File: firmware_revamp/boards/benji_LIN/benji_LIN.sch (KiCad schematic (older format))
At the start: 35 parts, among them J1 CONN_02X03, J2 Conn_01x11, J3 Conn_01x11, U1 MCP2561-E_SN, U2 ATMEGA16M1, U3 TLIN1021DRQ1, Y1 Crystal_SMD

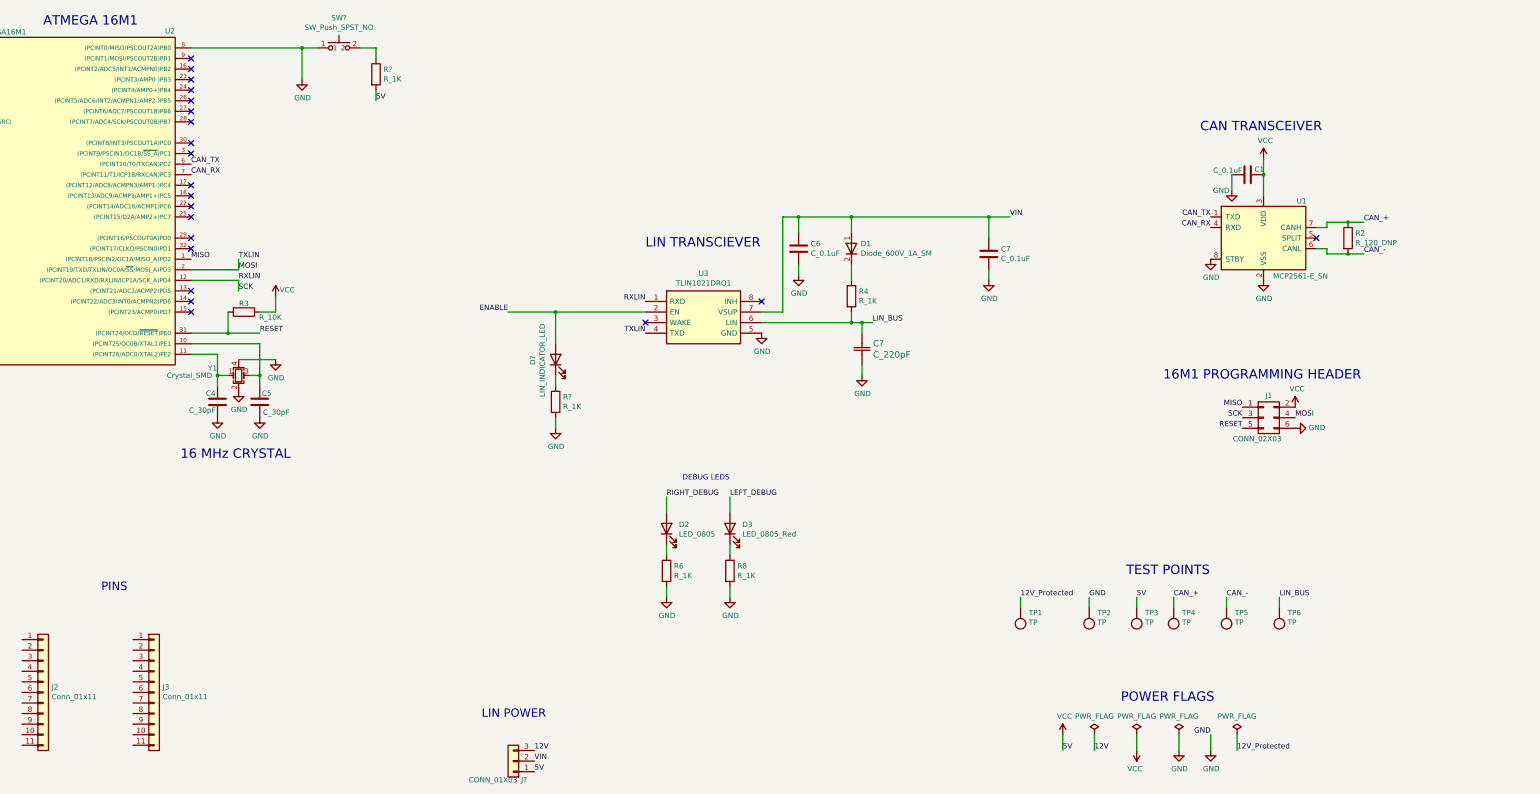
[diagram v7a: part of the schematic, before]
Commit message: Changed test points to smd
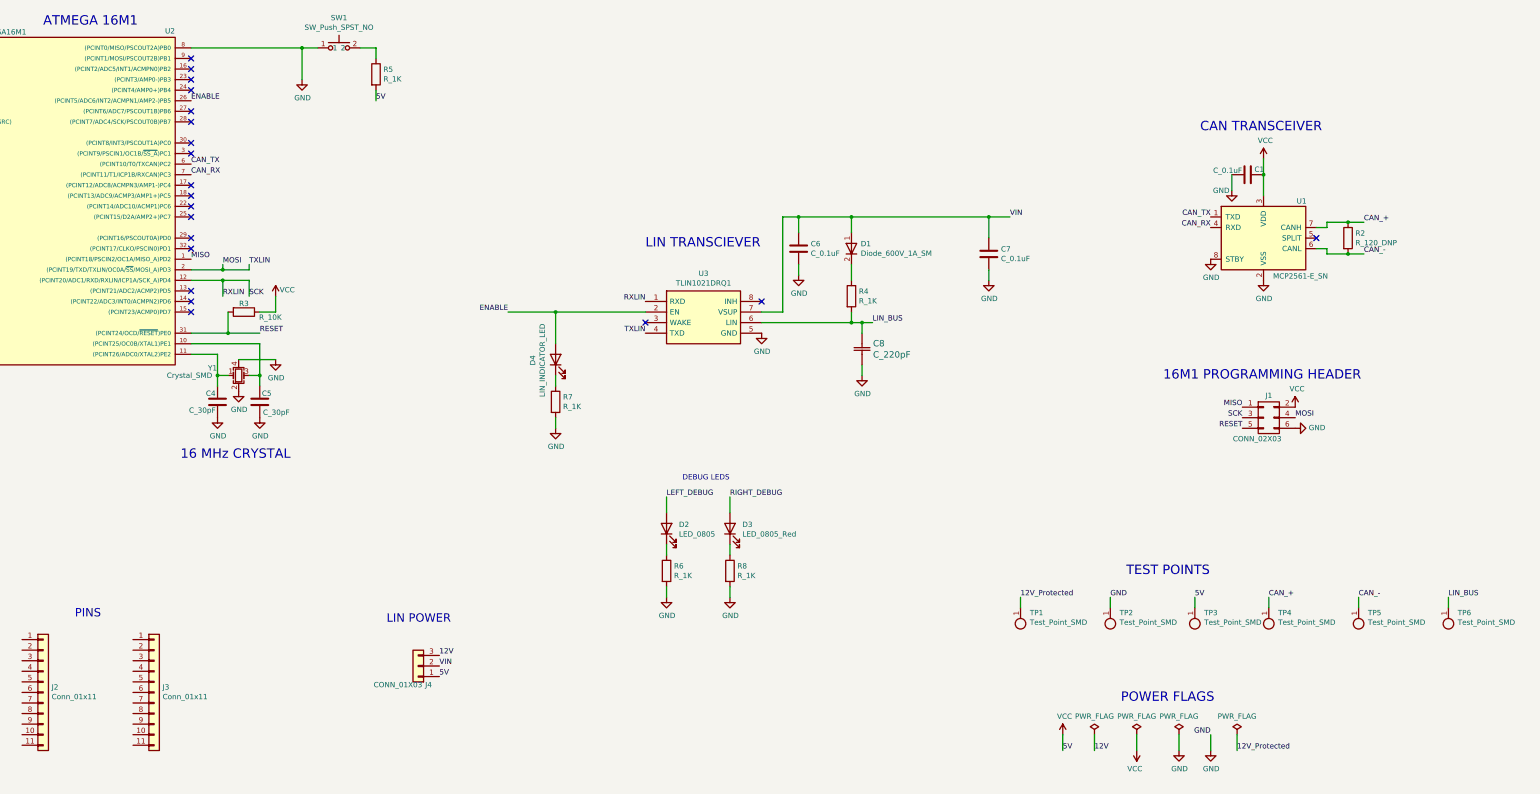
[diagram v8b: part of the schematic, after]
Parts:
- removed TP1, TP2, TP3, TP4, TP5, TP6: TP, footprints:tp_1.6mm, symbol formula:TP
- added TP1, TP2, TP3, TP4, TP5, TP6: Test_Point_SMD, footprints:Test_Point_SMD, symbol formula:Test_Point_SMD
- gave numbers to parts that had none: 6
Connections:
- net 12V_Protected: now also TP1.1
- net CAN_+: now also TP4.1
- net CAN_-: now also TP5.1
- net ENABLE: now also U2.26 ((PCINT5/ADC6/INT2/ACMPN1/AMP2-)PB5)
- net GND: now also TP2.1
- net LEFT_DEBUG: now also D2.2 (A); no longer D3.2 (A)
- net LIN_BUS: now also TP6.1
- net RIGHT_DEBUG: now also D3.2 (A); no longer D2.2 (A)
- net VCC: now also TP3.1
- no-connect marks 22 -> 21
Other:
- moved on the sheet: J4
